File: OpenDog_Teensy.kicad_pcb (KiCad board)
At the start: 2 copper layers, 61.6 x 96 mm, 42 parts, among them J1 NRF, J10 UART5, J11 UART6, J12 CAN1, J13 CAN2, J14 EXP, J15 Power, J2 TOF1, J3 TOF2, J4 IMU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

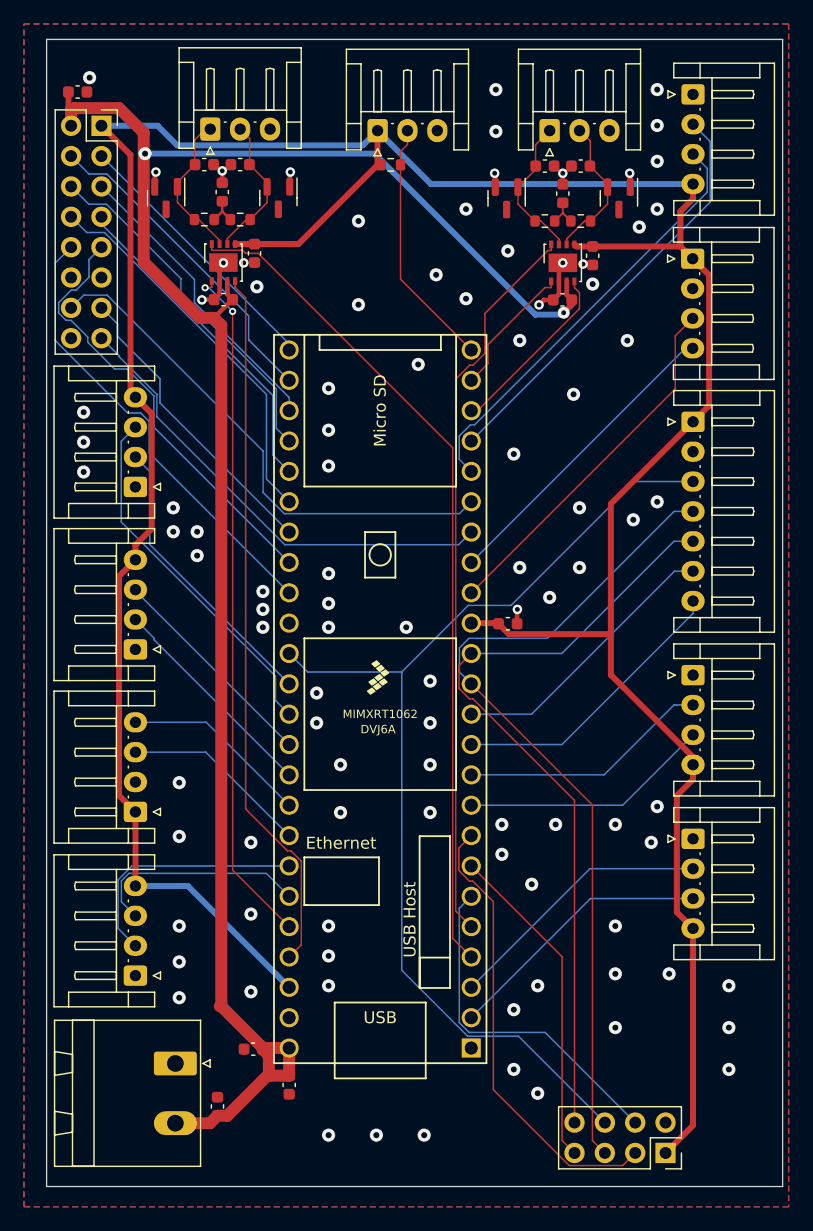
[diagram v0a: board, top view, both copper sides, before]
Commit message: Added labels to the silkscreen
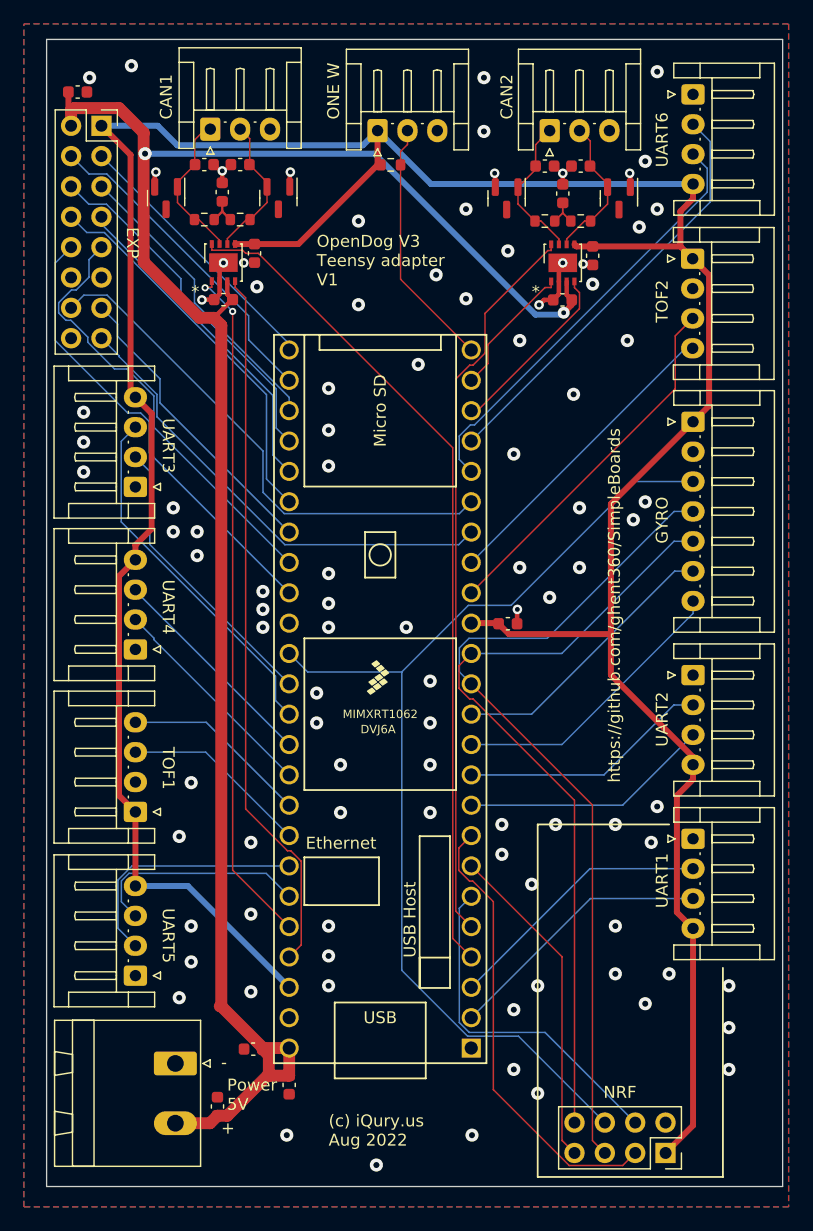
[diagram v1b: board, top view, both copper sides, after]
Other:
- board text added: "(c) iQury.us Aug 2022"
- board text added: "*"
- board text added: "+"
- board text added: "-"
- board text added: "-- --"
- board text added: "3.3V"
- board text added: "3.3V 5V"
- board text added: "3.3V GDN"
- board text added: "5V"
- board text added: "CAN1"
- board text added: "CAN2"
- board text added: "CS_BMP"
- board text added: "CS_IMU"
- board text added: "E1 E2"
- board text added: "E3 E4"
- board text added: "E5 E6"
- board text added: "E7 E8"
- board text added: "ENA CS"
- board text added: "EXP"
- board text added: "GND"
- board text added: "GYRO"
- board text added: "H"
- board text added: "L"
- board text added: "MISO"
- board text added: "MISO IRQ"
- board text added: "MISO SCK"
- board text added: "MOSI"
- board text added: "MOSI GND"
- board text added: "NRF"
- board text added: "ONE W"
- board text added: "OpenDog V3 Teensy adapter V1"
- board text added: "Power 5V"
- board text added: "RX"
- board text added: "SCK"
- board text added: "SCK MOSI"
- board text added: "SCL"
- board text added: "SDA"
- board text added: "TOF1"
- board text added: "TOF2"
- board text added: "TX"
- board text added: "UART1"
- board text added: "UART2"
- board text added: "UART3"
- board text added: "UART4"
- board text added: "UART5"
- board text added: "UART6"
- board text added: "https://github.com/ghent360/SimpleBoards"

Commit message: Added input voltage monitoring cirquit.
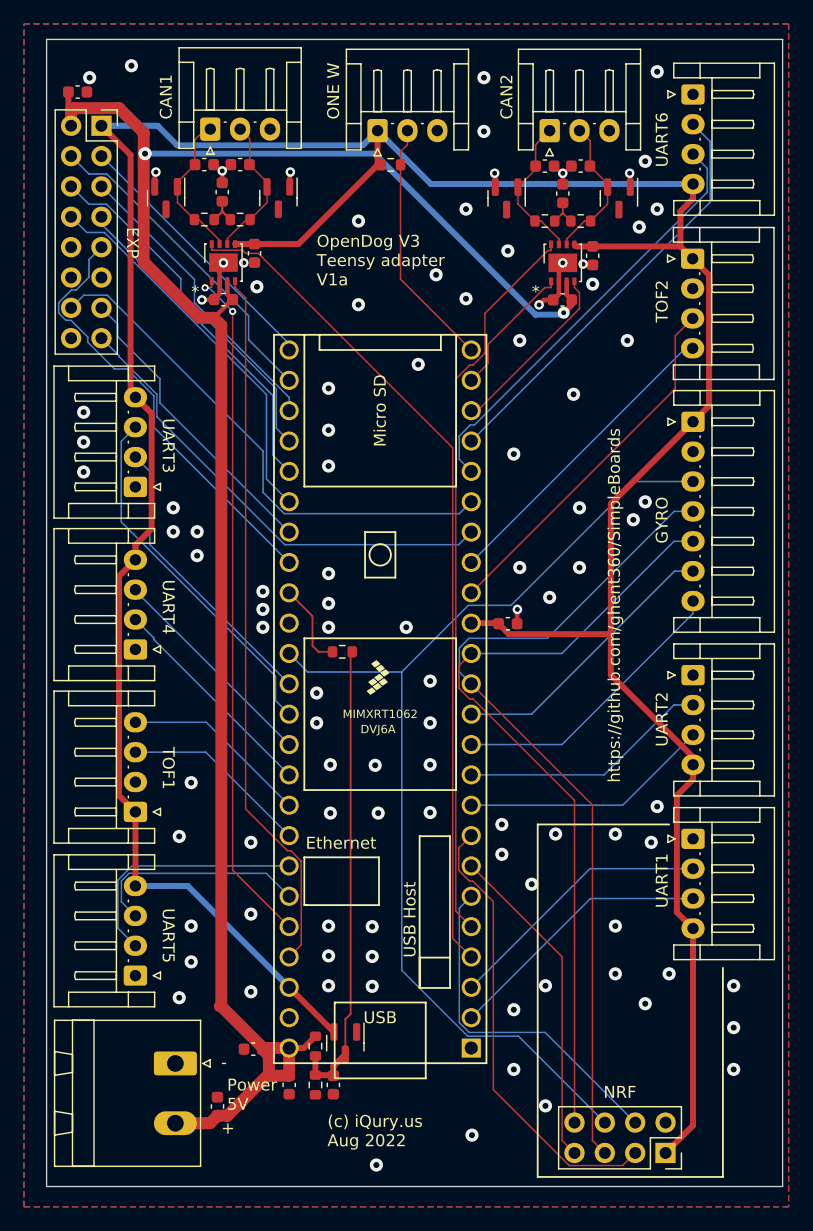
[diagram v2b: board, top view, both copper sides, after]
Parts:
- added C16: 100nF, Capacitor_SMD:C_0603_1608Metric, F.Cu at (57.9, 144.8)
- added D5: BAT54S, Package_TO_SOT_SMD:SOT-23, F.Cu at (58.9, 141.3)
- added R6: 4.7k, Resistor_SMD:R_0603_1608Metric, F.Cu at (56.4, 141.6)
- added R7: 2.2k, Resistor_SMD:R_0603_1608Metric, F.Cu at (56.4, 144.8)
- added R8: 10k, Resistor_SMD:R_0603_1608Metric, F.Cu at (58.6, 108.5)
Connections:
- J14 pad 10: /EXT8 -> unconnected-(J14-Pin_10)
- U1 pad 33: /EXT8 -> /V_MON
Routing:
- net Net-(C16-Pad1): track 0.00 -> 39.2 mm
- net /EXT8: track 38.2 -> 0.00 mm
- net /V_MON: track 0.00 -> 7.13 mm
- net /3.3V: track 265.7 -> 271.0 mm
- net /VIn: track 158.9 -> 161.5 mm
- net GND: vias 97 -> 101
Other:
- board text added: "E7 --"
- board text added: "OpenDog V3 Teensy adapter V1a"
- board text removed: "E7 E8"
- board text removed: "OpenDog V3 Teensy adapter V1"

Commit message: Improved routing.
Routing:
- net /VIn: track 161.5 -> 168.6 mm, vias 2 -> 1
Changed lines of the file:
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@@
   (segment (start 54.2 141.71) (end 54.2 144.025) (width 1) (layer "F.Cu") (net 1))
   (segment (start 39.967 63.048) (end 36.224919 63.048) (width 1) (layer "F.Cu") (net 1))
-  (segment (start 48.52291 138.218) (end 48.393 138.218) (width 1) (layer "F.Cu") (net 1))
   (segment (start 54.2 141.71) (end 52.065 141.71) (width 1) (layer "F.Cu") (net 1))
   (segment (start 35.95 64.525) (end 35.95 63.2977) (width 0.5) (layer "F.Cu") (net 1))
@@
   (segment (start 48.52291 81.22291) (end 47.9 80.6) (width 1) (layer "F.Cu") (net 1))
   (via (at 77.1762 80.1746) (size 1) (drill 0.4) (layers "F.Cu" "B.Cu") (net 1))
-  (via (at 42.1402 66.8598) (size 1.1) (drill 0.5) (layers "F.Cu" "B.Cu") (net 1))
   (segment (start 77.1762 80.1746) (end 77.0186 80.3322) (width 0.5) (layer "B.Cu") (net 1))
-  (segment (start 61.3404 66.8598) (end 42.1402 66.8598) (width 0.5) (layer "B.Cu") (net 1))
+  (segment (start 74.8128 80.3322) (end 61.3404 66.8598) (width 0.5) (layer "B.Cu") (net 1))
+  (segment (start 40.020041 66.8598) (end 38.912241 65.752) (width 0.5) (layer "B.Cu") (net 1))
+  (segment (start 37.177 65.752) (end 35.95 64.525) (width 0.5) (layer "B.Cu") (net 1))
+  (segment (start 38.912241 65.752) (end 37.177 65.752) (width 0.5) (layer "B.Cu") (net 1))
+  (segment (start 61.3404 66.8598) (end 40.020041 66.8598) (width 0.5) (layer "B.Cu") (net 1))
   (segment (start 77.0186 80.3322) (end 74.8128 80.3322) (width 0.5) (layer "B.Cu") (net 1))
-  (segment (start 74.8128 80.3322) (end 61.3404 66.8598) (width 0.5) (layer "B.Cu") (net 1))
   (segment (start 76.3 79.1) (end 75.5306 79.1) (width 0.381) (layer "F.Cu") (net 2))
   (segment (start 76.775 77.55) (end 76.775 76.325) (width 0.381) (layer "F.Cu") (net 2))

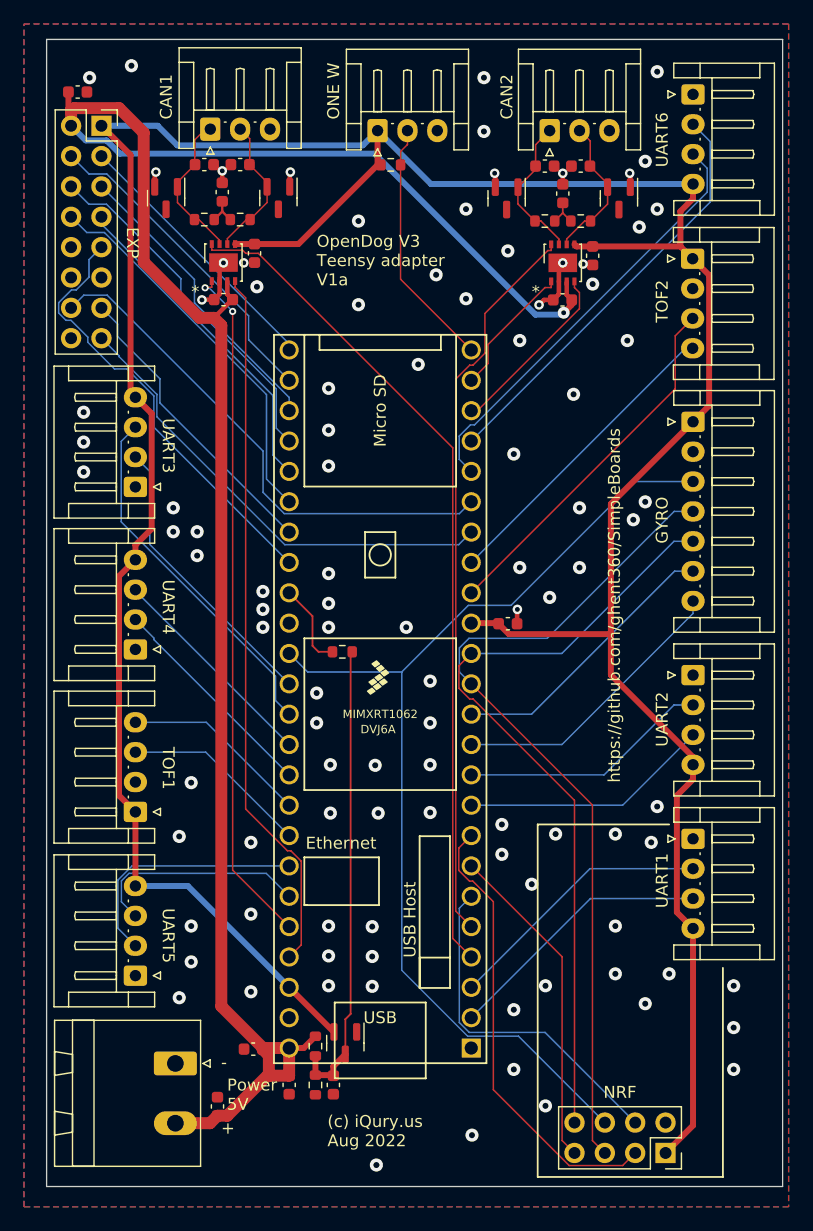
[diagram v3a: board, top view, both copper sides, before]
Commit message: Added more filtering capacitors on the 3.3v rail one for each connector.
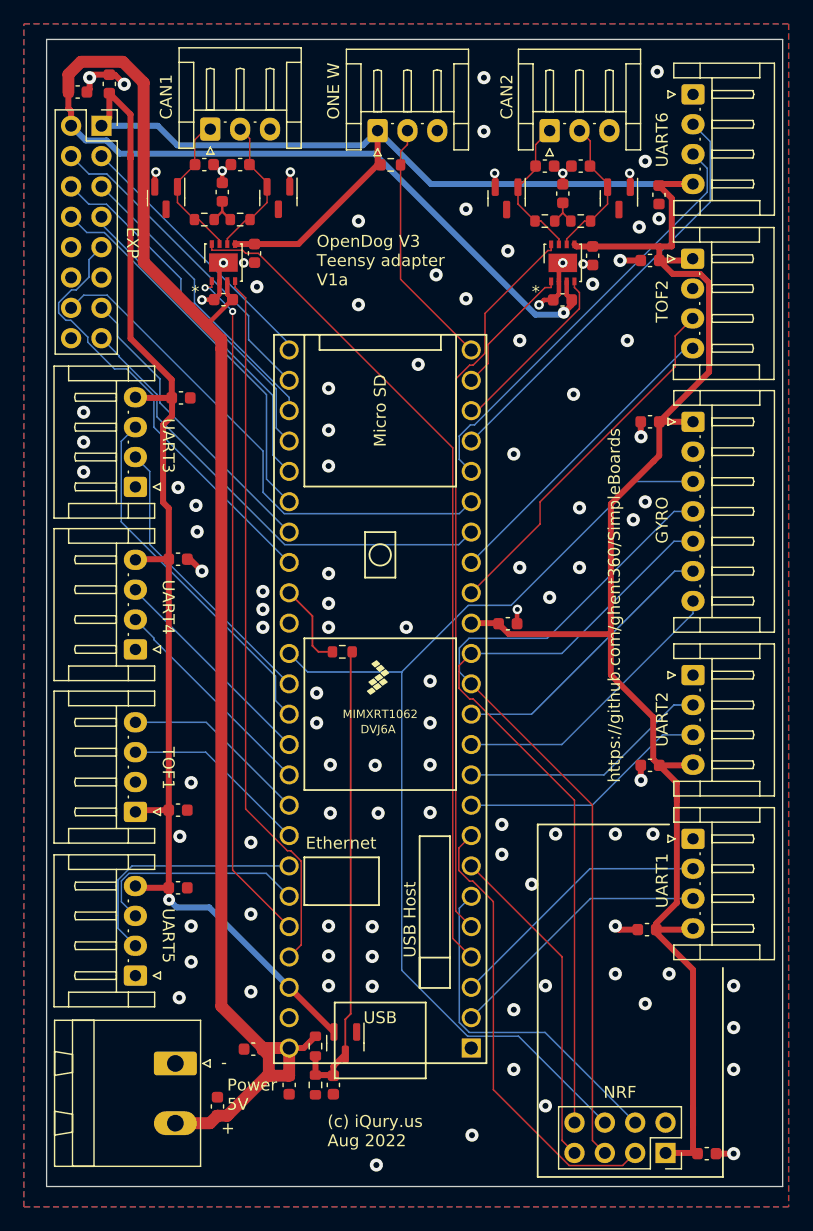
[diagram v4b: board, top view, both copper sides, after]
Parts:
- added C17: 100nF, Capacitor_SMD:C_0603_1608Metric, F.Cu at (39.1, 61.0)
- added C18: 100nF, Capacitor_SMD:C_0603_1608Metric, F.Cu at (84.4, 89.3)
- added C19: 100nF, Capacitor_SMD:C_0603_1608Metric, F.Cu at (84.4, 75.8)
- added C20: 100nF, Capacitor_SMD:C_0603_1608Metric, F.Cu at (84.4, 118.0)
- added C21: 100nF, Capacitor_SMD:C_0603_1608Metric, F.Cu at (84.2, 131.8)
- added C22: 100nF, Capacitor_SMD:C_0603_1608Metric, F.Cu at (85.2, 70.3)
- added C23: 100nF, Capacitor_SMD:C_0603_1608Metric, F.Cu at (44.9, 121.8)
- added C24: 100nF, Capacitor_SMD:C_0603_1608Metric, F.Cu at (89.2, 150.6)
- added C25: 100nF, Capacitor_SMD:C_0603_1608Metric, F.Cu at (44.9, 100.8)
- added C26: 100nF, Capacitor_SMD:C_0603_1608Metric, F.Cu at (44.9, 128.3)
- added C27: 100nF, Capacitor_SMD:C_0603_1608Metric, F.Cu at (45.1, 87.3)
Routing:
- net /3.3V: track 271.0 -> 306.4 mm, vias 0 -> 1
- net GND: track 17.3 -> 31.2 mm, vias 101 -> 104
- net /VIn: track 168.6 -> 173.6 mm
